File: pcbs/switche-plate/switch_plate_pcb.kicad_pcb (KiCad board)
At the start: 2 copper layers, 110.6 x 95.5 mm, 25 parts

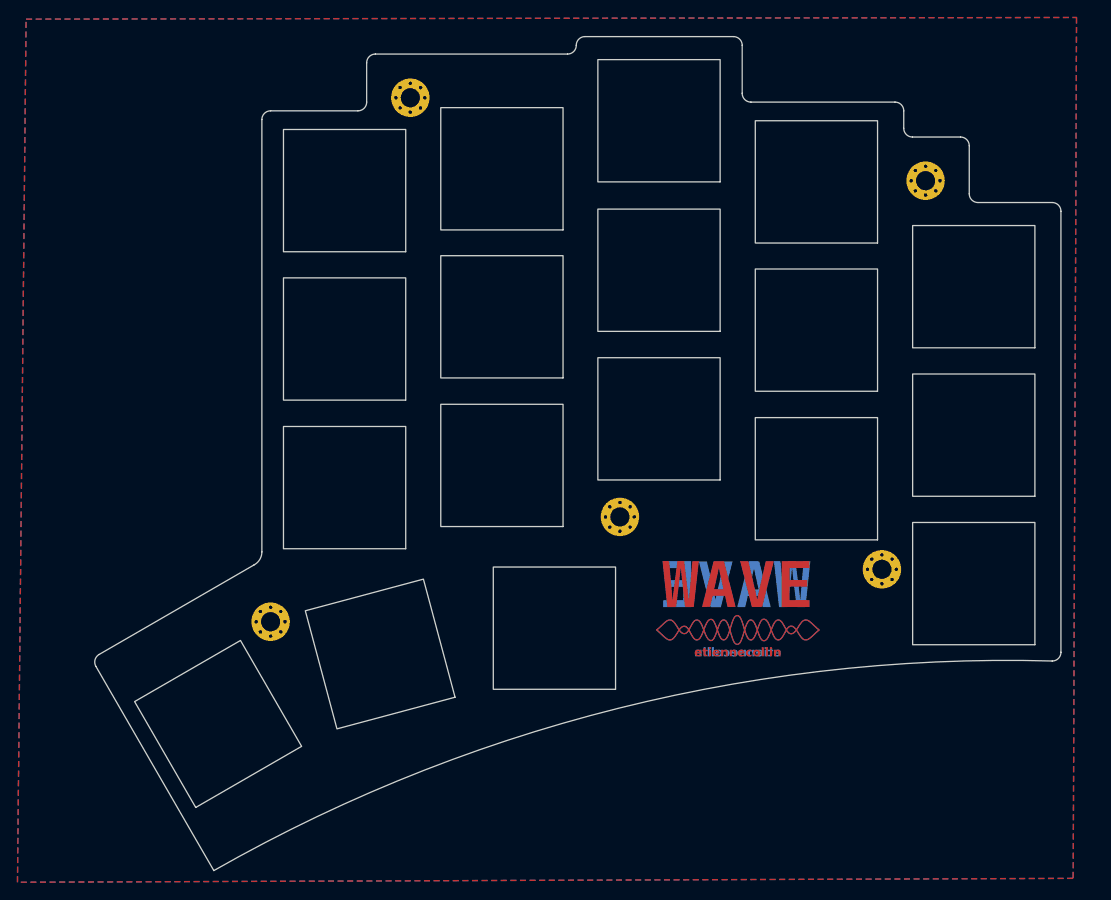
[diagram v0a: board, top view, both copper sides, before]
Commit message: Fixed spacing of PCB edges
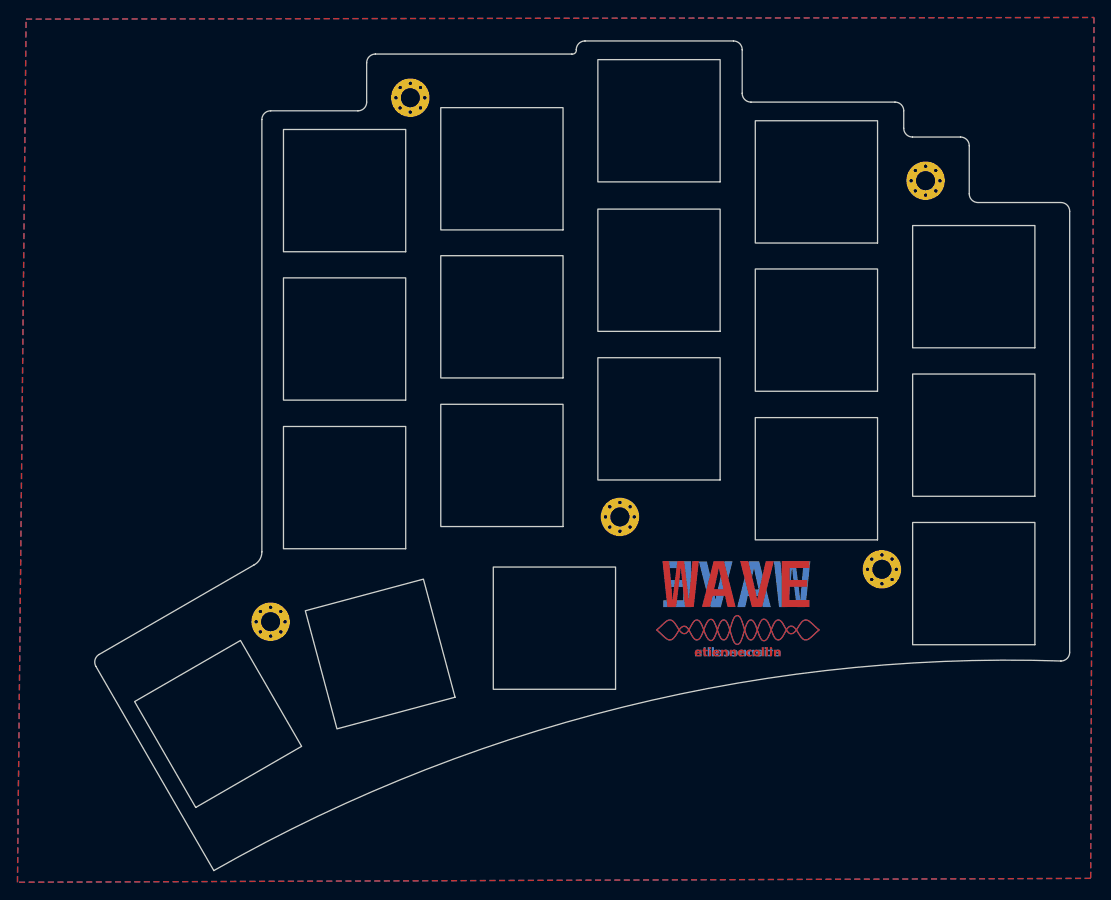
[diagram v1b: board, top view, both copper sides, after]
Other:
- board size 110.6 x 95.5 mm -> 111.6 x 95 mm
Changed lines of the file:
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@@
     (pad "1" thru_hole circle (at 1.65 0) (size 0.7 0.7) (drill 0.4) (layers "*.Cu" "*.Mask"))
   )
-  (gr_arc (start 144.5 41) (mid 145.207107 41.292893) (end 145.5 42)
+  (gr_arc (start 145.5 41) (mid 146.207107 41.292893) (end 146.5 42)
     (stroke (width 0.05) (type default)) (layer "Edge.Cuts"))
-  (gr_line (start 91 22) (end 108 22)
+  (gr_line (start 91 22.5) (end 108 22.5)
     (stroke (width 0.05) (type default)) (layer "Edge.Cuts"))
-  (gr_line (start 136 41) (end 144.5 41)
+  (gr_line (start 136 41) (end 145.5 41)
     (stroke (width 0.05) (type default)) (layer "Edge.Cuts"))
-  (gr_line (start 67 24) (end 89 24)
+  (gr_line (start 67 24) (end 89.5 24)
     (stroke (width 0.05) (type default)) (layer "Edge.Cuts"))
   (gr_arc (start 34.996172 94.118234) (mid 34.897043 93.357401) (end 35.366186 92.750279)
     (stroke (width 0.05) (type default)) (layer "Edge.Cuts"))
-  (gr_arc (start 48.5 117.5) (mid 94.852044 98.908178) (end 144.5 93.5)
+  (gr_arc (start 48.5 117.5) (mid 95.337204 98.779534) (end 145.5 93.5)
     (stroke (width 0.05) (type default)) (layer "Edge.Cuts"))
   (gr_line (start 127.5 32.5) (end 127.5 30.5)
     (stroke (width 0.05) (type default)) (layer "Edge.Cuts"))
-  (gr_arc (start 90 23) (mid 90.292893 22.292893) (end 91 22)
+  (gr_arc (start 90 23.5) (mid 90.292893 22.792893) (end 91 22.5)
     (stroke (width 0.05) (type default)) (layer "Edge.Cuts"))
   (gr_line (start 66 29.5) (end 66 25)
@@
   (gr_arc (start 66 25) (mid 66.292893 24.292893) (end 67 24)
     (stroke (width 0.05) (type default)) (layer "Edge.Cuts"))
-  (gr_line (start 145.5 42) (end 145.5 92.5)
+  (gr_line (start 146.5 42) (end 146.5 92.5)
     (stroke (width 0.05) (type default)) (layer "Edge.Cuts"))
   (gr_arc (start 128.5 33.5) (mid 127.792893 33.207107) (end 127.5 32.5)
     (stroke (width 0.05) (type default)) (layer "Edge.Cuts"))
-  (gr_arc (start 145.5 92.5) (mid 145.207107 93.207107) (end 144.5 93.5)
+  (gr_arc (start 146.5 92.5) (mid 146.207107 93.207107) (end 145.5 93.5)
     (stroke (width 0.05) (type default)) (layer "Edge.Cuts"))
   (gr_arc (start 110 29.5) (mid 109.292893 29.207107) (end 109 28.5)
@@
   (gr_arc (start 126.5 29.5) (mid 127.207107 29.792893) (end 127.5 30.5)
     (stroke (width 0.05) (type default)) (layer "Edge.Cuts"))
-  (gr_line (start 109 23) (end 109 28.5)
+  (gr_line (start 109 23.5) (end 109 28.5)
     (stroke (width 0.05) (type default)) (layer "Edge.Cuts"))
   (gr_arc (start 54 81) (mid 53.757738 81.874643) (end 53.1 82.5)
@@
   (gr_line (start 54 81) (end 54 31.5)
     (stroke (width 0.05) (type default)) (layer "Edge.Cuts"))
-  (gr_arc (start 108 22) (mid 108.707107 22.292893) (end 109 23)
+  (gr_arc (start 108 22.5) (mid 108.707107 22.792893) (end 109 23.5)
     (stroke (width 0.05) (type default)) (layer "Edge.Cuts"))
   (gr_arc (start 54 31.5) (mid 54.292893 30.792893) (end 55 30.5)
@@
   (gr_line (start 110 29.5) (end 126.5 29.5)
     (stroke (width 0.05) (type default)) (layer "Edge.Cuts"))
-  (gr_arc (start 90 23) (mid 89.707107 23.707107) (end 89 24)
+  (gr_arc (start 90 23.5) (mid 89.875 23.875) (end 89.5 24)
     (stroke (width 0.05) (type default)) (layer "Edge.Cuts"))
   (zone (net 0) (net_name "") (layers "F&B.Cu") (name "Ground") (hatch edge 0.508)
@@
     (polygon
       (pts
-        (xy 147.285298 19.809186)
-        (xy 146.901563 118.389311)
+        (xy 149.285298 19.809186)
+        (xy 148.901563 118.389311)
         (xy 26.012915 118.834236)
         (xy 27 20)
